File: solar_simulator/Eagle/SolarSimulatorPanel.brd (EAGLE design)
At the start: 150 x 70 mm, 105 parts, among them J1 DCJ0202, J2 DCJ0202

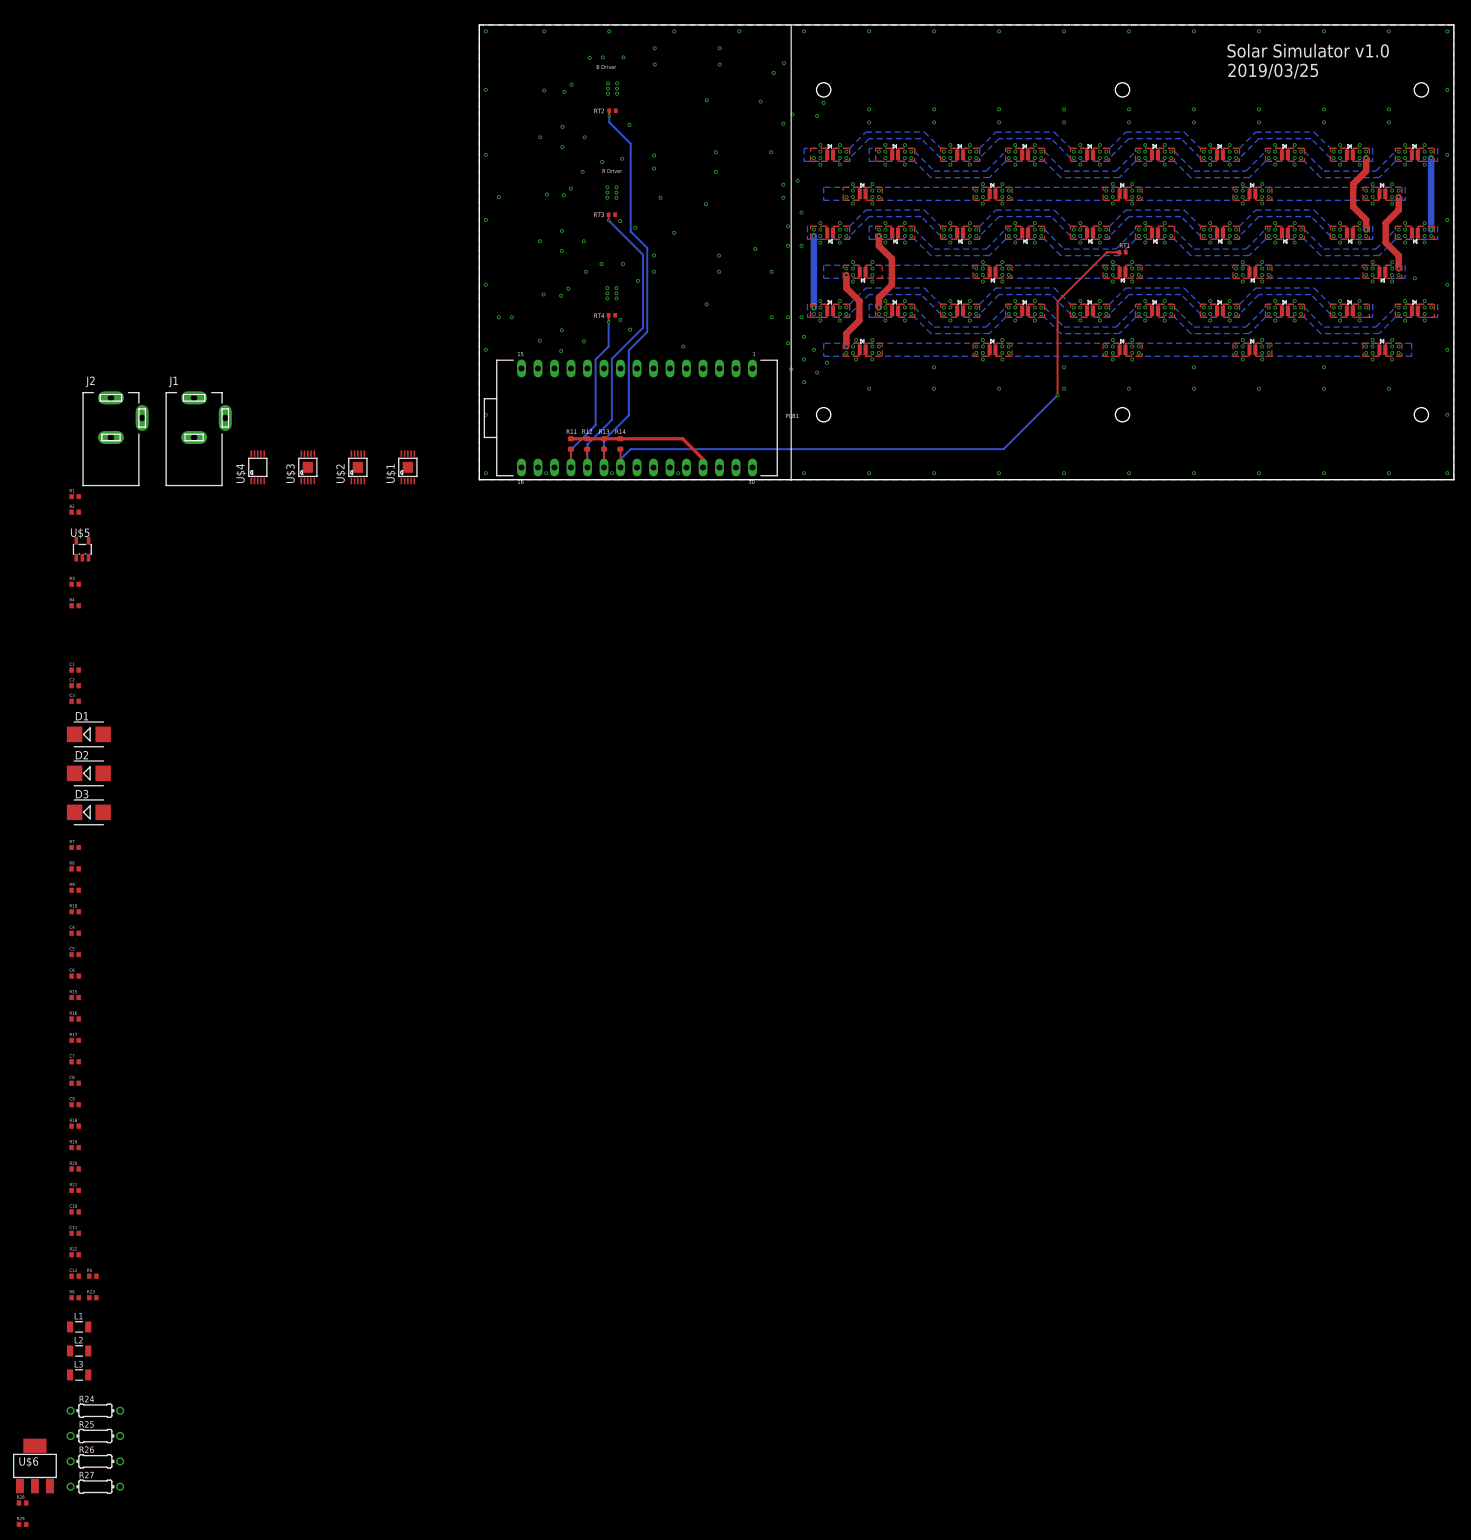
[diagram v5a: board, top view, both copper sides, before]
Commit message: added solar simulator rev 2.0, moved eagle files to oresat eagle repo
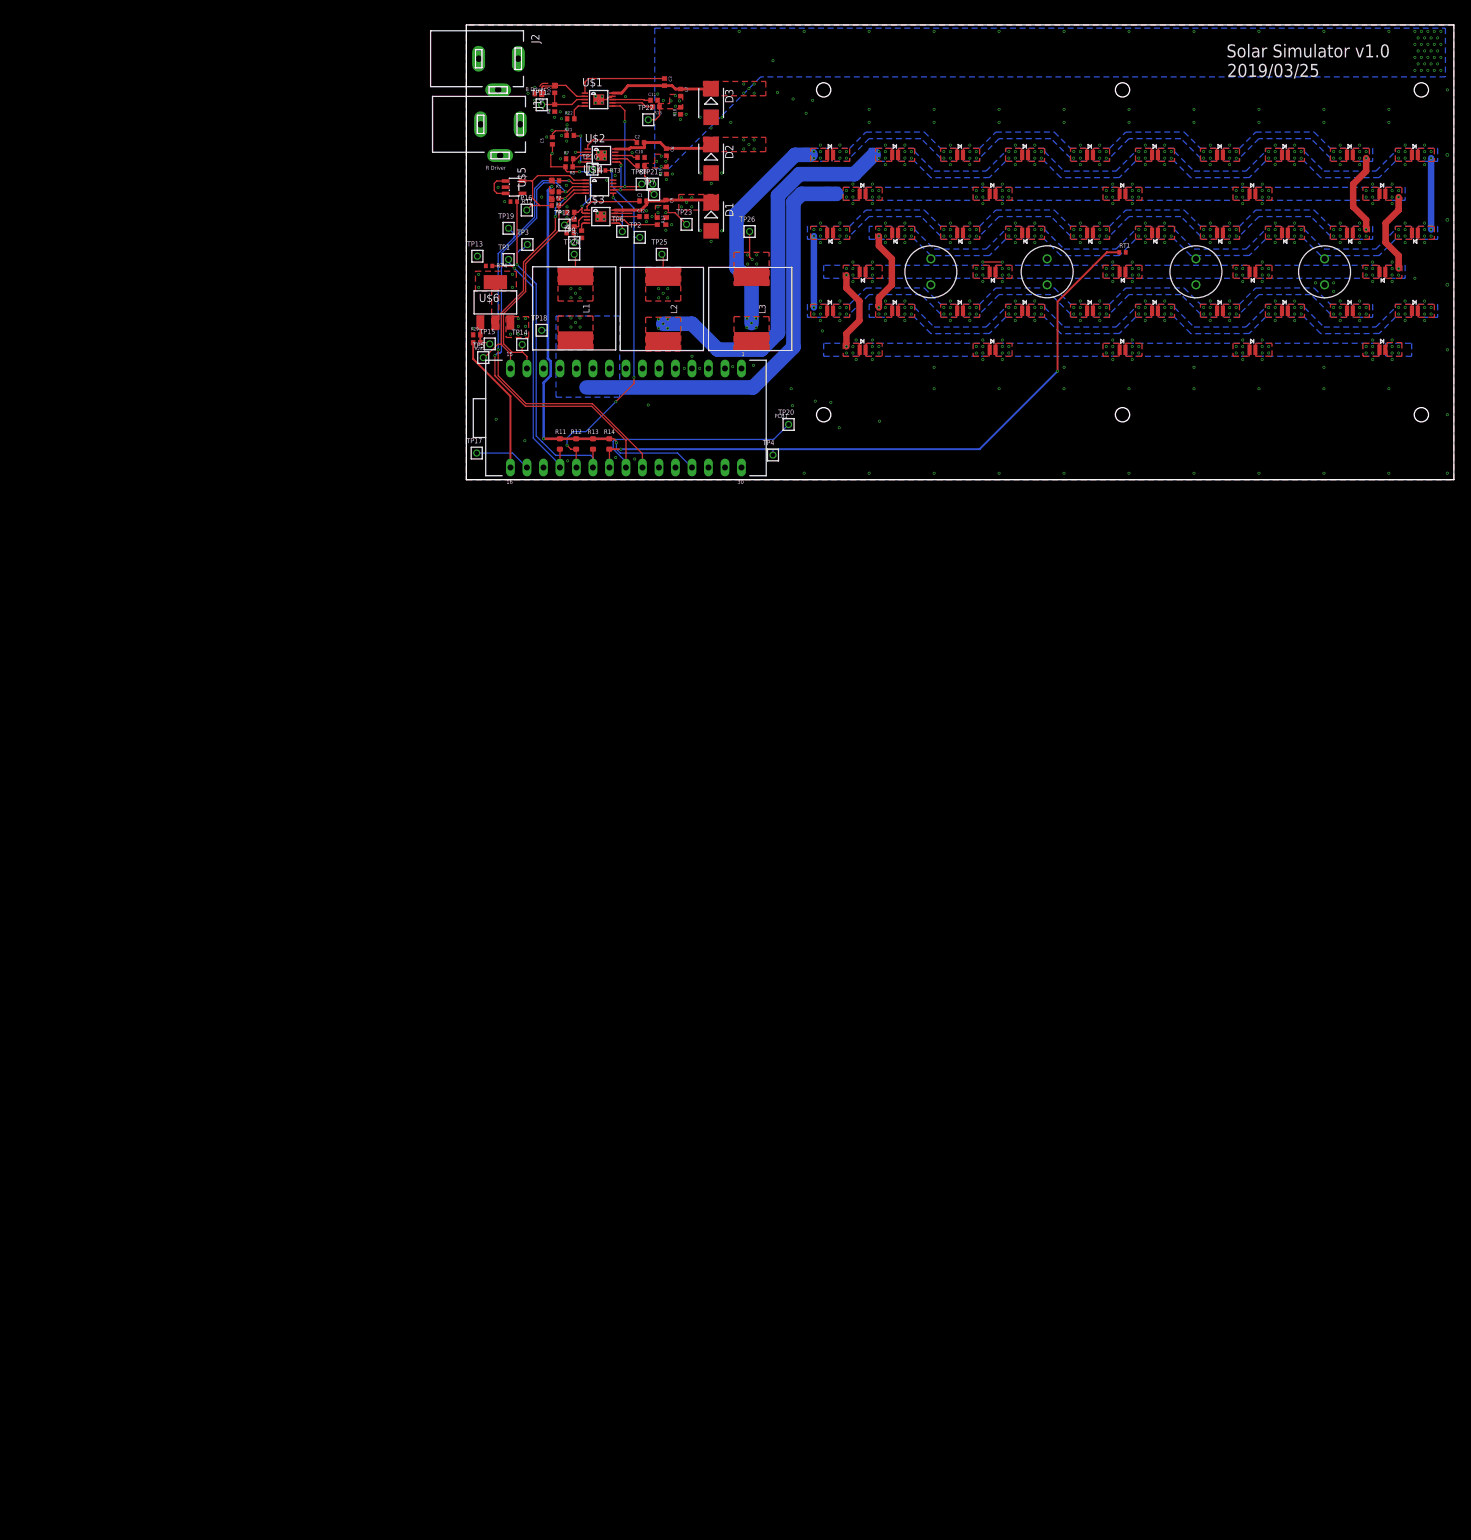
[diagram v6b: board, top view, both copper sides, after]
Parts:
- removed R24, R25, R26, R27: (no value), oresat-rcl:0204/7
- added TP1, TP10, TP11, TP12, TP13, TP14, TP15, TP16, TP17, TP18, TP19, TP2, TP20, TP21, TP22, TP23, TP24, TP25, TP26, TP3, TP4, TP5, TP6, TP7, TP8, TP9: TEST-POINT, Tova:2MM-TEST-POINT
- added U$10, U$7, U$8, U$9: HL_G4BULB, HL_HalogenBulb_G4Base:G4BASE
- BLUE1, BLUE10, BLUE11, BLUE12, BLUE13, BLUE14, BLUE15, BLUE2, BLUE3, BLUE4, BLUE5, BLUE6, BLUE7, BLUE8, BLUE9, GREE9, GREEN1, GREEN10, GREEN11, GREEN12, GREEN13, GREEN14, GREEN15, GREEN2, GREEN3, GREEN4, GREEN5, GREEN6, GREEN7, GREEN8, RED1, RED10, RED11, RED12, RED13, RED14, RED15, RED2, RED3, RED4, RED5, RED6, RED7, RED8, RED9: device solarsim:X-QE -> D-Cree-XQE-LED:X-QE
- C10, C11, C12: value TBD -> .1u
- C7, C8, C9: value TBD -> .15u
- D1, D2, D3: value TBD -> (none)
- L1, L2, L3: value TBD -> 170u; device oresat-rcl:1206-C -> L_Wurst_7447709681:1212NONSTANDARD
- R21, R22, R23: value TBD -> 11k
- moved R29 196.0 mm to (-0.40, 22.3)
- moved C11 195.8 mm to (26.9, 58.4)
- moved L3 193.9 mm to (41.9, 26.2), turned to 270 degrees
- moved U$6 192.6 mm to (2.47, 27.3)
- moved R28 191.8 mm to (-0.40, 21.1), turned to 180 degrees
- moved R22 190.8 mm to (14.1, 55.6)
- moved C12 185.0 mm to (25.2, 40.5)
- moved C10 184.2 mm to (24.9, 49.6)
- moved L2 183.8 mm to (28.3, 26.2), turned to 270 degrees
- moved R6 182.4 mm to (14.6, 39.5), turned to 90 degrees
- moved R18 182.0 mm to (31.0, 56.8), turned to 90 degrees
- moved R23 180.1 mm to (15.7, 37.8), turned to 90 degrees
- moved R21 179.4 mm to (14.0, 53.0)
- moved R5 176.6 mm to (14.0, 38.0)
- moved C7 175.9 mm to (31.0, 59.6), turned to 270 degrees
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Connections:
- removed net +12: J1.3
- removed net +56V: J2.3
- removed net N$60: C8.1
- removed net N$62: C9.1
- net +3V3: now also TP17.1
- net +5V: now also TP18.1
- net A0: now also TP1.1
- net A1: now also TP2.1
- net A2: now also TP3.1
- net A3: now also TP4.1
- net GND: now also U$10.G2; no longer R27.2
- net N$1: now also TP20.1
- net N$18: now also TP7.1
- net N$22: now also L3.P$1, TP26.1; no longer L3.1
- net N$24: now also C8.1, L2.P$1, TP25.1; no longer L2.1
- net N$25: now also C9.1, L1.P$1, TP24.1; no longer L1.1
- net N$28: now also TP14.1
- net N$3: now also TP19.1
- net N$32: now also TP5.1
- net N$4: now also TP16.1
- net N$52: now also TP10.1
- net N$53: now also TP11.1
- net N$59: now also TP21.1
- net N$6: now also TP9.1
- net N$61: now also TP23.1
- net N$64: now also TP8.1
- net N$68: now also TP6.1
- net N$69: now also L1.P$2; no longer L1.2
- net N$70: now also L2.P$2; no longer L2.2
- net N$71: now also TP22.1
- net N$72: now also L3.P$2; no longer L3.2
- net N$73: now also U$7.G1; no longer R24.1
- net N$74: now also U$7.G2, U$8.G1; no longer R24.2, R25.1
- net N$75: now also U$8.G2, U$9.G1; no longer R25.2, R26.1
- net N$76: now also U$10.G1, U$9.G2; no longer R26.2, R27.1
- net N$78: now also TP15.1
- net VCC: now also J1.3, TP13.1
- net VCC/2: now also J2.3, TP12.1
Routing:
- net N$1: track 0.00 -> 102.9 mm, vias 0 -> 2
- net N$3: track 0.00 -> 72.3 mm, vias 0 -> 2
- net N$69: track 0.00 -> 63.9 mm, vias 0 -> 9
- net N$70: track 0.00 -> 58.8 mm, vias 0 -> 9
- net +5V: track 21.6 -> 66.0 mm, vias 0 -> 3
- net N$32: track 0.00 -> 39.2 mm, vias 0 -> 2
- net N$28: track 0.00 -> 37.2 mm
- net N$72: track 0.00 -> 33.0 mm, vias 0 -> 9
- net VCC/2: track 0.00 -> 24.3 mm, vias 0 -> 4
- net N$79: track 0.00 -> 21.6 mm
- net N$22: track 0.00 -> 20.4 mm, vias 0 -> 10
- net N$24: track 0.00 -> 19.9 mm, vias 0 -> 10
- net N$25: track 0.00 -> 19.4 mm, vias 0 -> 10
- net N$4: track 0.00 -> 18.9 mm
- net N$64: track 0.00 -> 18.5 mm, vias 0 -> 2
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- added copper zone on layer 1, net +5V
- added copper zone on layer 15, net GND
- added copper zone on layer 1, net N$22
- added copper zone on layer 2, net N$22
- added copper zone on layer 1, net N$24
- added copper zone on layer 2, net N$24
- added copper zone on layer 1, net N$25
- added copper zone on layer 2, net N$25
- added copper zone on layer 1, net N$59
- added copper zone on layer 16, net N$59
- added copper zone on layer 2, net N$59
- added copper zone on layer 1, net N$61
- added copper zone on layer 16, net N$61
- added copper zone on layer 2, net N$61
- added copper zone on layer 1, net N$69
- added copper zone on layer 16, net N$69
- added copper zone on layer 1, net N$70
- added copper zone on layer 16, net N$70
- added copper zone on layer 1, net N$71
- added copper zone on layer 16, net N$71
- added copper zone on layer 2, net N$71
- added copper zone on layer 1, net N$72
- added copper zone on layer 16, net N$72
- added copper zone on layer 1, net N$73
- added copper zone on layer 2, net N$73
- added copper zone on layer 2, net N$74
- added copper zone on layer 2, net N$75
- added copper zone on layer 2, net N$76
- added copper zone on layer 1, net VCC
- added copper zone on layer 2, net VCC
- added copper zone on layer 2, net VCC/2
- added copper zone on layer 1, net VCC/3
- removed copper zone on layer 1, net BLUE-OUT
- removed copper zone on layer 16, net BLUE-OUT
- removed copper zone on layer 1, net BLUE-RTN
- removed copper zone on layer 16, net BLUE-RTN
- removed copper zone on layer 1, net GREEN-RTN
- removed copper zone on layer 16, net GREEN-RTN
- removed copper zone on layer 1, net GRN-OUT
- removed copper zone on layer 16, net GRN-OUT
- removed copper zone on layer 1, net RED-OUT
- removed copper zone on layer 16, net RED-OUT
- removed copper zone on layer 1, net RED-RTN
- removed copper zone on layer 16, net RED-RTN
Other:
- board size 150 x 70 mm -> 152 x 70 mm
- board text removed: "CON"

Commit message: rev 2.1 of solar simulator
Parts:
- removed R28: 220, oresat-rcl:.0402-A-NOSILK
- removed U$5: AP2127, U-Diodes-AP2127-LDO:SOT23-5
- added C13, C14, C15: 10u, rcl:C2220K
- added TP27, TP28, TP29, TP30: TEST-POINT, Tova:2MM-TEST-POINT
- C1: value .1 u -> 100n
- C12, C2, C4, C5, C6: value .1u -> 100n
- C7, C8, C9: value .15u -> 150n; device oresat-rcl:.0402-A-NOSILK -> rcl:C0805K
- J1: value DCJ0202 -> PJ-102B; device con-jack:DCJ0202 -> J-CUI-PJ102B-Barrel_Jack:CUI_PJ-102B
- J2: value DCJ0202 -> RAPC722BKZ-TH; device con-jack:DCJ0202 -> J-SwitchCraft-RAPC722BKZ-Barrel_Jack:RAPC722BKZ
- PCB1: device solarsim:ARDUINO_NANO_SHIELD -> U-Arduino-Nano-DevBoard:ARDUINO_NANO_SHIELD
- R1, R2: value 10k -> 4.7k
- R18, R19, R20: value TBD -> 300m; device oresat-rcl:.0402-A-NOSILK -> rcl:R0805
- RT1, RT2, RT3, RT4: device solarsim:R0402 -> R-Generic-Thermister0402:R0402
- U$1, U$2, U$3: value TPS92512 -> (none)
- moved J1 48.8 mm to (2.50, 5.90), turned to 180 degrees
- moved L3 38.2 mm to (33.6, 63.5), turned to 0 degrees
- moved TP13 31.6 mm to (11.4, 5.00)
- moved TP14 31.1 mm to (6.00, 51.9)
- moved U$6 28.6 mm to (20.7, 5.30)
- moved R1 27.8 mm to (8.85, 18.3), turned to 270 degrees
- moved RT2 26.7 mm to (15.7, 67.4)
- moved TP26 26.4 mm to (25.6, 59.2)
- moved R2 26.0 mm to (9.88, 18.4), turned to 270 degrees
- moved R29 25.8 mm to (15.7, 2.20)
- moved R3 25.0 mm to (11.0, 18.4), turned to 270 degrees
- moved L2 24.7 mm to (33.6, 50.3), turned to 0 degrees
- moved TP12 22.2 mm to (-0.30, 56.9)
- moved L1 21.5 mm to (33.6, 36.8), turned to 0 degrees
- moved TP18 21.1 mm to (25.5, 9.20)
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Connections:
- net N$1 renamed SDA
- net N$3 renamed SCL
- net N$32 renamed !LDAC
- removed net N$73: U$6.3, U$7.G1
- removed net N$74: U$7.G2, U$8.G1
- removed net N$75: U$8.G2, U$9.G1
- removed net N$76: U$10.G1, U$9.G2
- removed net N$78: R28.1, R29.2, TP15.1, U$6.1
- removed net VCC: J1.3, TP13.1, U$6.2, U$6.4
- removed net VCC/2: C4.1, C5.1, J2.3, R6.2, R8.2, TP12.1, U$2.2, U$3.2
- removed net VCC/3: C6.1, R10.2, U$1.2
- new net !RESET: PCB1.28, PCB1.3, TP27.1
- new net 12V: J1.2, TP13.1, U$6.2, U$6.4
- new net 56V: C13.1, C14.1, C15.1, C4.1, C5.1, C6.1, J2.SLEEVE, R10.2, R6.2, R8.2, TP12.1, U$1.2, U$2.2, U$3.2
- new net N$62: U$10.G1, U$6.3, U$7.G1, U$8.G1, U$9.G1
- new net N$84: TP30.1, U$3.4
- new net N$85: TP28.1, U$2.4
- new net N$86: TP29.1, U$1.4
- net GND: now also C13.2, C14.2, C15.2, J2.CENTER, U$7.G2, U$8.G2, U$9.G2; no longer J2.1, U$5.2
- net N$22: no longer C7.1
- net N$24: no longer C8.1
- net N$25: no longer C9.1
- net N$4: no longer TP16.1, U$5.5
- net N$69: now also C9.1
- net N$70: now also C8.1
- net N$72: now also C7.1
- net N$79: now also R29.2, TP15.1, U$6.1; no longer R28.2
- net N$80: now also TP16.1, U$4.9; no longer U$5.1, U$5.3
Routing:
- net N$69: track 63.9 -> 22.6 mm, vias 9 -> 0
- net N$70: track 58.8 -> 26.8 mm, vias 9 -> 0
- net +5V: track 66.0 -> 35.6 mm, vias 3 -> 1
- net !RESET: track 0.00 -> 26.4 mm
- net N$59: track 3.32 -> 28.1 mm, vias 40 -> 34
- net N$71: track 3.38 -> 27.7 mm, vias 8 -> 29
- net VCC/2: track 24.3 -> 0.00 mm, vias 4 -> 0
- net A2: track 55.7 -> 76.6 mm
- net N$68: track 8.68 -> 28.5 mm, vias 1 -> 2
- net N$61: track 3.95 -> 22.7 mm, vias 7 -> 12
- net N$4: track 18.9 -> 1.33 mm
- net 56V: track 0.00 -> 14.6 mm, vias 0 -> 32
- net N$25: track 19.4 -> 6.55 mm, vias 10 -> 0
- net N$34: track 14.2 -> 2.09 mm
- net N$22: track 20.4 -> 9.32 mm, vias 10 -> 0
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- added copper zone on layer 1, net 12V
- added copper zone on layer 15, net 12V
- added copper zone on layer 1, net 56V
- added copper zone on layer 15, net 56V
- added copper zone on layer 2, net GND
- added copper zone on layer 15, net N$59
- added copper zone on layer 15, net N$61
- added copper zone on layer 1, net N$62
- added copper zone on layer 15, net N$62
- added copper zone on layer 15, net N$71
- removed copper zone on layer 1, net +5V
- removed copper zone on layer 15, net GND
- removed copper zone on layer 2, net N$22
- removed copper zone on layer 2, net N$24
- removed copper zone on layer 2, net N$25
- removed copper zone on layer 2, net N$59
- removed copper zone on layer 2, net N$61
- removed copper zone on layer 16, net N$69
- removed copper zone on layer 16, net N$70
- removed copper zone on layer 2, net N$71
- removed copper zone on layer 16, net N$72
- removed copper zone on layer 1, net N$73
- removed copper zone on layer 2, net N$73
- removed copper zone on layer 2, net N$74
- removed copper zone on layer 2, net N$75
- removed copper zone on layer 2, net N$76
- removed copper zone on layer 1, net VCC
- removed copper zone on layer 2, net VCC
- removed copper zone on layer 2, net VCC/2
- removed copper zone on layer 1, net VCC/3
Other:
- board text removed: "R Driver"
